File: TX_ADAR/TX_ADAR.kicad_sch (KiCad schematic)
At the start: 22 parts, among them J19 Conn_Coaxial, J20 Conn_Coaxial, SW5 SW_Push, SW8 SW_Push, U2 ADAR2001ACCZ

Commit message: Got footprints to work
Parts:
- J19, J20: footprint (none) -> 142_1701_831:BEL_142-1701-831
- U2: footprint ADAR_footprints:LGA-CC-40-7_ADI -> ADAR footprints:LGA-CC-40-7_ADI
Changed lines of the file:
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@@
 			)
 		)
-		(property "Footprint" "ADAR_footprints:LGA-CC-40-7_ADI"
+		(property "Footprint" "ADAR footprints:LGA-CC-40-7_ADI"
 			(at 176.53 25.4 0)
 			(hide yes)
@@
 			)
 		)
-		(property "Footprint" ""
+		(property "Footprint" "142_1701_831:BEL_142-1701-831"
 			(at 76.2 158.75 0)
 			(hide yes)
@@
 			)
 		)
-		(property "Footprint" ""
+		(property "Footprint" "142_1701_831:BEL_142-1701-831"
 			(at 34.29 158.75 0)
 			(hide yes)

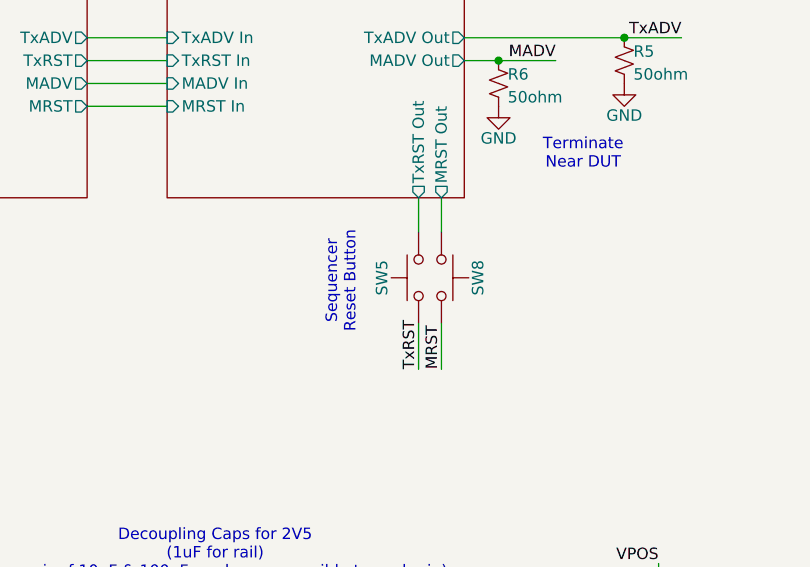
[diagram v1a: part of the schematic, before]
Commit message: Finished up adding footprints. Removed unnecessary switches for the TxRST and MRST
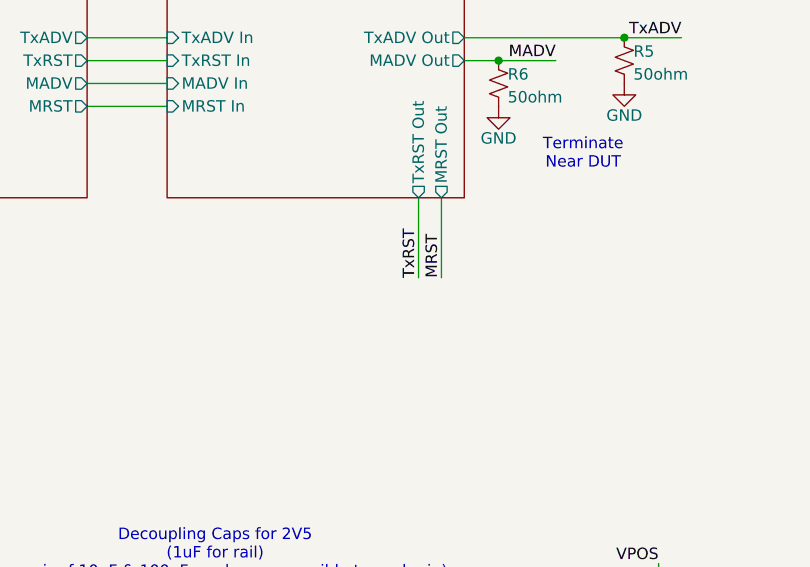
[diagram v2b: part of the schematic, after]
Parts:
- removed SW5, SW8: SW_Push, symbol Switch:SW_Push
- C12, C13, C16, C32, C33, C34, C35, C36, C37, C8, C9: footprint (none) -> Capacitor_SMD:C_0603_1608Metric_Pad1.08x0.95mm_HandSolder
- R5, R6: footprint (none) -> Resistor_SMD:R_0603_1608Metric_Pad0.98x0.95mm_HandSolder
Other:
- note removed: "Sequencer Reset Button"
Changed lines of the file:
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@@
 		)
 	)
-	(text "Sequencer\nReset Button"
-		(exclude_from_sim no)
-		(at 73.914 97.028 90)
-		(effects
-			(font
-				(size 1.27 1.27)
-			)
-		)
-	)
 	(text "Thru Cal Line\nLength = 2 x RF Output"
 		(exclude_from_sim no)
@@
 	(wire
 		(pts
-			(xy 82.55 101.6) (xy 82.55 106.68)
+			(xy 82.55 87.63) (xy 82.55 96.52)
 		)
 		(stroke
@@
 	(wire
 		(pts
-			(xy 85.09 87.63) (xy 85.09 91.44)
+			(xy 85.09 87.63) (xy 85.09 96.52)
 		)
 		(stroke
@@
 	(wire
 		(pts
-			(xy 82.55 87.63) (xy 82.55 91.44)
-		)
-		(stroke
-			(width 0)
-			(type default)
-		)
-	)
-	(wire
-		(pts
 			(xy 231.14 55.88) (xy 231.14 48.26)
 		)
@@
 	(wire
 		(pts
-			(xy 85.09 101.6) (xy 85.09 106.68)
-		)
-		(stroke
-			(width 0)
-			(type default)
-		)
-	)
-	(wire
-		(pts
 			(xy 167.64 58.42) (xy 176.53 58.42)
 		)
@@
 	)
 	(label "TxRST"
-		(at 82.55 106.68 90)
+		(at 82.55 96.52 90)
 		(effects
 			(font
@@
 	)
 	(label "MRST"
-		(at 85.09 106.68 90)
+		(at 85.09 96.52 90)
 		(effects
 			(font
@@
 			)
 		)
-		(property "Footprint" ""
+		(property "Footprint" "Capacitor_SMD:C_0603_1608Metric_Pad1.08x0.95mm_HandSolder"
 			(at 139.3952 45.72 0)
 			(hide yes)
@@
 			)
 		)
-		(property "Footprint" ""
+		(property "Footprint" "Capacitor_SMD:C_0603_1608Metric_Pad1.08x0.95mm_HandSolder"
 			(at 50.4952 138.43 0)
 			(hide yes)
@@
 	)
 	(symbol
-		(lib_id "Switch:SW_Push")
-		(at 82.55 96.52 90)
-		(unit 1)
-		(body_style 1)
-		(exclude_from_sim no)
-		(in_bom yes)
-		(on_board yes)
-		(in_pos_files yes)
-		(dnp no)
-		(property "Reference" "SW5"
-			(at 78.486 96.52 0)
-			(show_name no)
-			(do_not_autoplace no)
-			(effects
-				(font
-					(size 1.27 1.27)
-				)
-			)
-		)
-		(property "Value" "SW_Push"
-			(at 77.47 96.52 0)
-			(hide yes)
-			(show_name no)
-			(do_not_autoplace no)
-			(effects
-				(font
-					(size 1.27 1.27)
-				)
-			)
-		)
-		(property "Footprint" ""
-			(at 77.47 96.52 0)
-			(hide yes)
-			(show_name no)
-			(do_not_autoplace no)
-			(effects
-				(font
-					(size 1.27 1.27)
-				)
-			)
-		)
-		(property "Datasheet" ""
-			(at 77.47 96.52 0)
-			(hide yes)
-			(show_name no)
-			(do_not_autoplace no)
-			(effects
-				(font
-					(size 1.27 1.27)
-				)
-			)
-		)
-		(property "Description" "Push button switch, generic, two pins"
-			(at 82.55 96.52 0)
-			(hide yes)
-			(show_name no)
-			(do_not_autoplace no)
-			(effects
-				(font
-					(size 1.27 1.27)
-				)
-			)
-		)
-		(pin "2"
-		)
-		(pin "1"
-		)
-		(instances
-			(project "TX_ADAR"
-				(path "/5bb7bcfe-c6dc-48dd-b109-2cc47fd52212"
-					(reference "SW5")
-					(unit 1)
-				)
-			)
-		)
-	)
-	(symbol
 		(lib_id "Device:C")
 		(at 109.22 134.62 0)
@@
 			)
 		)
-		(property "Footprint" ""
+		(property "Footprint" "Capacitor_SMD:C_0603_1608Metric_Pad1.08x0.95mm_HandSolder"
 			(at 110.1852 138.43 0)
 			(hide yes)
@@
 			)
 		)
-		(property "Footprint" ""
+		(property "Footprint" "Capacitor_SMD:C_0603_1608Metric_Pad1.08x0.95mm_HandSolder"
 			(at 61.9252 138.43 0)
 			(hide yes)
@@
 			)
 		)
-		(property "Footprint" ""
+		(property "Footprint" "Capacitor_SMD:C_0603_1608Metric_Pad1.08x0.95mm_HandSolder"
 			(at 74.6252 138.43 0)
 			(hide yes)
@@
 			)
 		)
-		(property "Footprint" ""
+		(property "Footprint" "Capacitor_SMD:C_0603_1608Metric_Pad1.08x0.95mm_HandSolder"
 			(at 152.0952 45.72 0)
 			(hide yes)
@@
 			)
 		)
-		(property "Footprint" ""
+		(property "Footprint" "Resistor_SMD:R_0603_1608Metric_Pad0.98x0.95mm_HandSolder"
 			(at 105.41 72.39 0)
 			(hide yes)
@@
 			)
 		)
-		(property "Footprint" ""
+		(property "Footprint" "Capacitor_SMD:C_0603_1608Metric_Pad1.08x0.95mm_HandSolder"
 			(at 37.7952 138.43 0)
 			(hide yes)
@@
 			)
 		)
-		(property "Footprint" ""
+		(property "Footprint" "Resistor_SMD:R_0603_1608Metric_Pad0.98x0.95mm_HandSolder"
 			(at 91.44 74.93 0)
 			(hide yes)
@@
 			)
 		)
-		(property "Footprint" ""
+		(property "Footprint" "Capacitor_SMD:C_0603_1608Metric_Pad1.08x0.95mm_HandSolder"
 			(at 16.2052 138.43 0)
 			(hide yes)
@@
 	)
 	(symbol
-		(lib_id "Switch:SW_Push")
-		(at 85.09 96.52 270)
-		(unit 1)
-		(body_style 1)
-		(exclude_from_sim no)
-		(in_bom yes)
-		(on_board yes)
-		(in_pos_files yes)
-		(dnp no)
-		(property "Reference" "SW8"
-			(at 89.154 96.52 0)
-			(show_name no)
-			(do_not_autoplace no)
-			(effects
-				(font
-					(size 1.27 1.27)
-				)
-			)
-		)
-		(property "Value" "SW_Push"
-			(at 90.17 96.52 0)
-			(hide yes)
-			(show_name no)
-			(do_not_autoplace no)
-			(effects
-				(font
-					(size 1.27 1.27)
-				)
-			)
-		)
-		(property "Footprint" ""
-			(at 90.17 96.52 0)
-			(hide yes)
-			(show_name no)
-			(do_not_autoplace no)
-			(effects
-				(font
-					(size 1.27 1.27)
-				)
-			)
-		)
-		(property "Datasheet" ""
-			(at 90.17 96.52 0)
-			(hide yes)
-			(show_name no)
-			(do_not_autoplace no)
-			(effects
-				(font
-					(size 1.27 1.27)
-				)
-			)
-		)
-		(property "Description" "Push button switch, generic, two pins"
-			(at 85.09 96.52 0)
-			(hide yes)
-			(show_name no)
-			(do_not_autoplace no)
-			(effects
-				(font
-					(size 1.27 1.27)
-				)
-			)
-		)
-		(pin "2"
-		)
-		(pin "1"
-		)
-		(instances
-			(project "TX_ADAR"
-				(path "/5bb7bcfe-c6dc-48dd-b109-2cc47fd52212"
-					(reference "SW8")
-					(unit 1)
-				)
-			)
-		)
-	)
-	(symbol
 		(lib_id "Connector:Conn_Coaxial")
 		(at 34.29 158.75 0)
@@
 			)
 		)
-		(property "Footprint" ""
+		(property "Footprint" "Capacitor_SMD:C_0603_1608Metric_Pad1.08x0.95mm_HandSolder"
 			(at 26.3652 138.43 0)
 			(hide yes)
@@
 			)
 		)
-		(property "Footprint" ""
+		(property "Footprint" "Capacitor_SMD:C_0603_1608Metric_Pad1.08x0.95mm_HandSolder"
 			(at 86.0552 138.43 0)
 			(hide yes)
@@
 			)
 		)
-		(property "Footprint" ""
+		(property "Footprint" "Capacitor_SMD:C_0603_1608Metric_Pad1.08x0.95mm_HandSolder"
 			(at 98.7552 138.43 0)
 			(hide yes)

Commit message: Layout Updates
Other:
- sheet SPI Communications ports: added OE; removed none
- sheet Sequencer Level Shifter ports: added OE; removed none
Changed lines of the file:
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@@
 	)
 	(junction
+		(at 90.17 31.75)
+		(diameter 0)
+		(color 0 0 0 0)
+	)
+	(junction
 		(at 231.14 33.02)
 		(diameter 0)
@@
 	)
 	(junction
-		(at 90.17 31.75)
-		(diameter 0)
-		(color 0 0 0 0)
-	)
-	(junction
 		(at 231.14 68.58)
 		(diameter 0)
@@
 	(wire
 		(pts
+			(xy 91.44 31.75) (xy 90.17 31.75)
+		)
+		(stroke
+			(width 0)
+			(type default)
+		)
+	)
+	(wire
+		(pts
 			(xy 227.33 71.12) (xy 231.14 71.12)
 		)
@@
 	(wire
 		(pts
-			(xy 90.17 31.75) (xy 90.17 62.23)
+			(xy 91.44 31.75) (xy 91.44 62.23)
 		)
 		(stroke
@@
 	(wire
 		(pts
-			(xy 90.17 62.23) (xy 87.63 62.23)
+			(xy 91.44 62.23) (xy 87.63 62.23)
 		)
 		(stroke
@@
 	(wire
 		(pts
+			(xy 88.9 34.29) (xy 88.9 64.77)
+		)
+		(stroke
+			(width 0)
+			(type default)
+		)
+	)
+	(wire
+		(pts
 			(xy 45.72 31.75) (xy 49.53 31.75)
 		)
@@
 	(wire
 		(pts
+			(xy 87.63 64.77) (xy 88.9 64.77)
+		)
+		(stroke
+			(width 0)
+			(type default)
+		)
+	)
+	(wire
+		(pts
 			(xy 231.14 33.02) (xy 227.33 33.02)
 		)
@@
 	(wire
 		(pts
+			(xy 87.63 34.29) (xy 88.9 34.29)
+		)
+		(stroke
+			(width 0)
+			(type default)
+		)
+	)
+	(wire
+		(pts
 			(xy 176.53 27.94) (xy 172.72 27.94)
 		)
@@
 			)
 		)
+		(pin "OE" output
+			(at 87.63 34.29 0)
+			(effects
+				(font
+					(size 1.27 1.27)
+				)
+				(justify right)
+			)
+		)
 		(instances
 			(project "TX_ADAR"
@@
 			)
 		)
+		(pin "OE" input
+			(at 87.63 64.77 0)
+			(effects
+				(font
+					(size 1.27 1.27)
+				)
+				(justify right)
+			)
+		)

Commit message: Layout comments and slight changes
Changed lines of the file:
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@@
 	)
 	(junction
-		(at 90.17 31.75)
+		(at 91.44 31.75)
 		(diameter 0)
 		(color 0 0 0 0)
@@
 	(wire
 		(pts
-			(xy 91.44 31.75) (xy 90.17 31.75)
-		)
-		(stroke
-			(width 0)
-			(type default)
-		)
-	)
-	(wire
-		(pts
 			(xy 227.33 71.12) (xy 231.14 71.12)
 		)
@@
 	(wire
 		(pts
-			(xy 90.17 31.75) (xy 87.63 31.75)
+			(xy 87.63 31.75) (xy 91.44 31.75)
 		)
 		(stroke
@@
 	(symbol
 		(lib_id "power:+1V8")
-		(at 90.17 31.75 0)
+		(at 91.44 31.75 0)
 		(unit 1)
 		(body_style 1)
@@
 		(dnp no)
 		(property "Reference" "#PWR02"
-			(at 90.17 35.56 0)
+			(at 91.44 35.56 0)
 			(hide yes)
 			(show_name no)
@@
 		)
 		(property "Value" "+1V8"
-			(at 90.17 27.94 0)
+			(at 91.44 27.94 0)
 			(show_name no)
 			(do_not_autoplace no)
@@
 		)
 		(property "Footprint" ""
-			(at 90.17 31.75 0)
+			(at 91.44 31.75 0)
 			(hide yes)
 			(show_name no)
@@
 		)
 		(property "Datasheet" ""
-			(at 90.17 31.75 0)
+			(at 91.44 31.75 0)
 			(hide yes)
 			(show_name no)
@@
 		)
 		(property "Description" "Power symbol creates a global label with name \"+1V8\""
-			(at 90.17 31.75 0)
+			(at 91.44 31.75 0)
 			(hide yes)
 			(show_name no)

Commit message: Got layout feedback from flatrim
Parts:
- removed J19, J20: Conn_Coaxial, 142_1701_831:BEL_142-1701-831, symbol Connector:Conn_Coaxial
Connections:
- no-connect marks 2 -> 0
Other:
- sheet SPI Communications ports: added none; removed 1V8SDIO2, 1V8SDIO3
- note removed: "Thru Cal Line Length = 2 x RF Output"

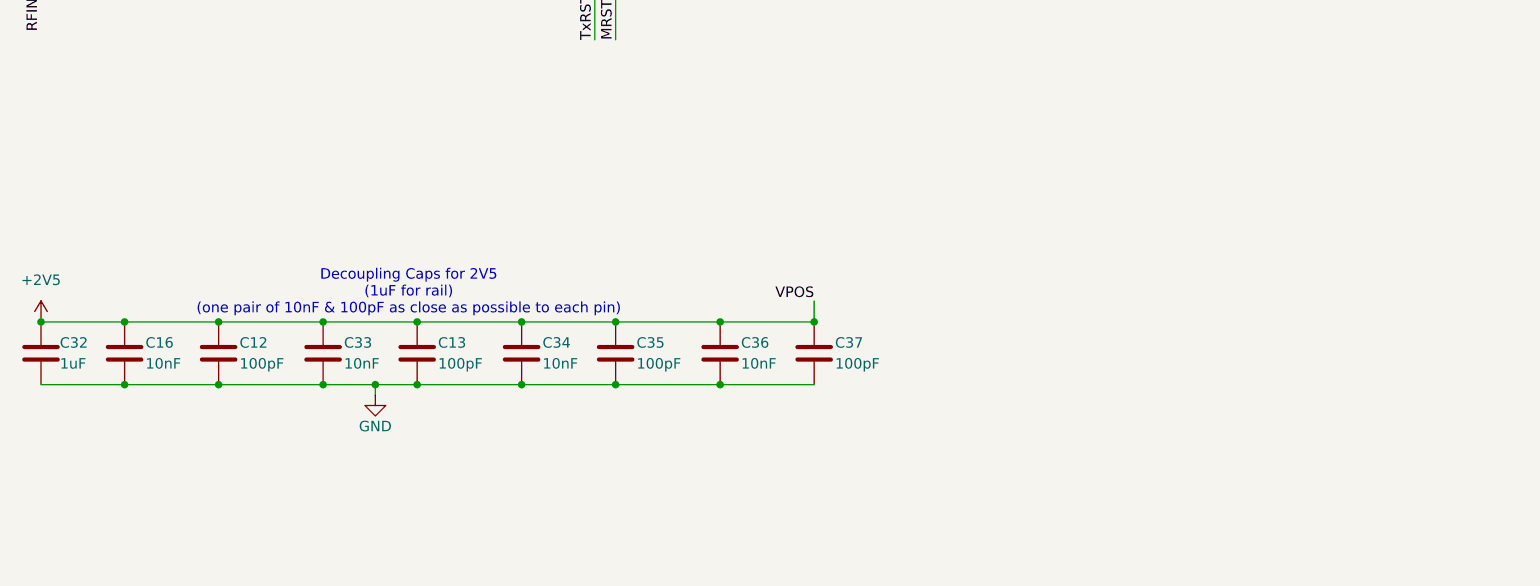
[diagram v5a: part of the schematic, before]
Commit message: Fixed tracks & added images to schem
NEED: Find 50 ohm impedance width for OSH Park
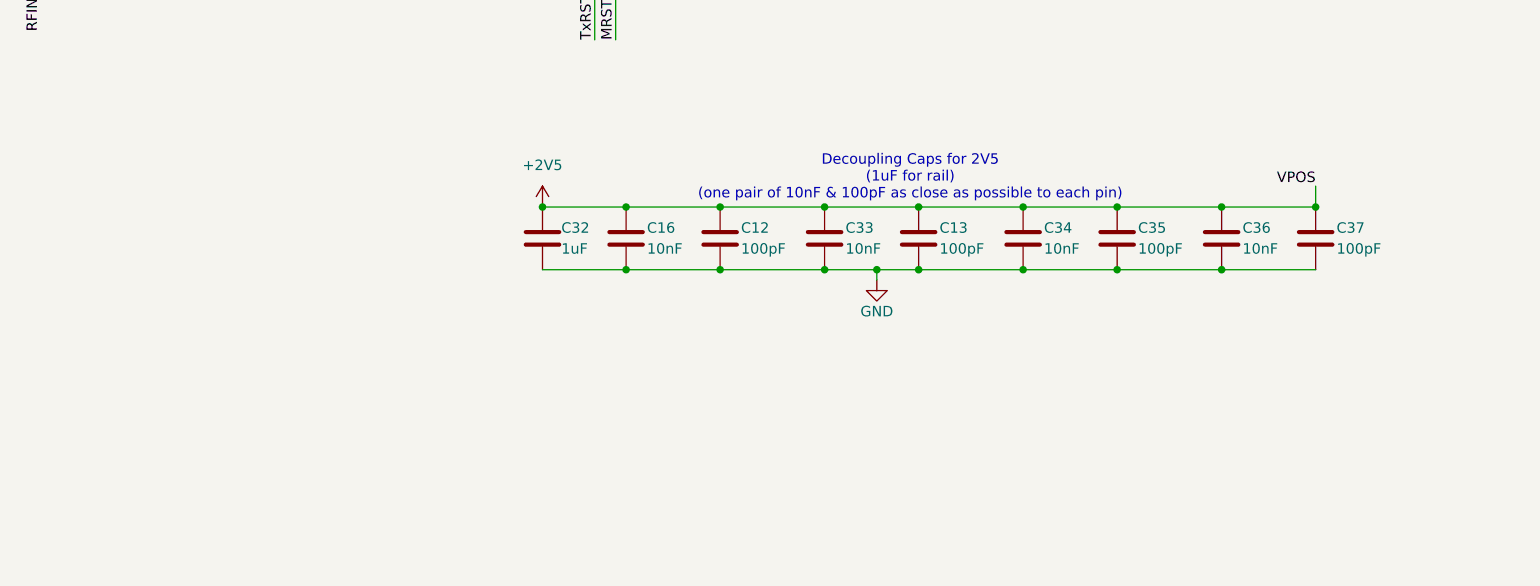
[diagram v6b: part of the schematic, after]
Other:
- moved on the sheet: C12, C13, C16, C32, C33, C34, C35, C36, C37
